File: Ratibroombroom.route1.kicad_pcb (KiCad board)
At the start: 2 copper layers, 46 x 60 mm, 112 parts, among them J1 Conn_01x02_Male, J10 Conn_01x04_Male, J11 Conn_01x04_Male, J2 Conn_01x02_Male, J3 Conn_01x10_Male, J5 Conn_01x02_Male, J6 Conn_01x02_Male, J8 Conn_01x04_Male, J9 Conn_01x04_Male, Q1 IRLML6344, Q10 S8050, Q11 IRF7416PbF, Q2 IRLML6344, Q3 IRLML6344, Q4 IRLML6344, Q5 PT12-21B/TR8, Q6 PT12-21B/TR8, Q7 PT12-21B/TR8, Q8 PT12-21B/TR8, Q9 IRLML6344, SW1 B3U, SW2 B3U, SW3 PCM12, U1 AZ1117-3.3, U2 DRV8835, U3 AS5145B-HSST, U4 MPU-9250, U5 STM32F405RGTx, U6 AS5145B-HSST, U7 DRV8835, U8 L6932D1.2TR, U9 L6932D1.2TR, Y1 8MHZ

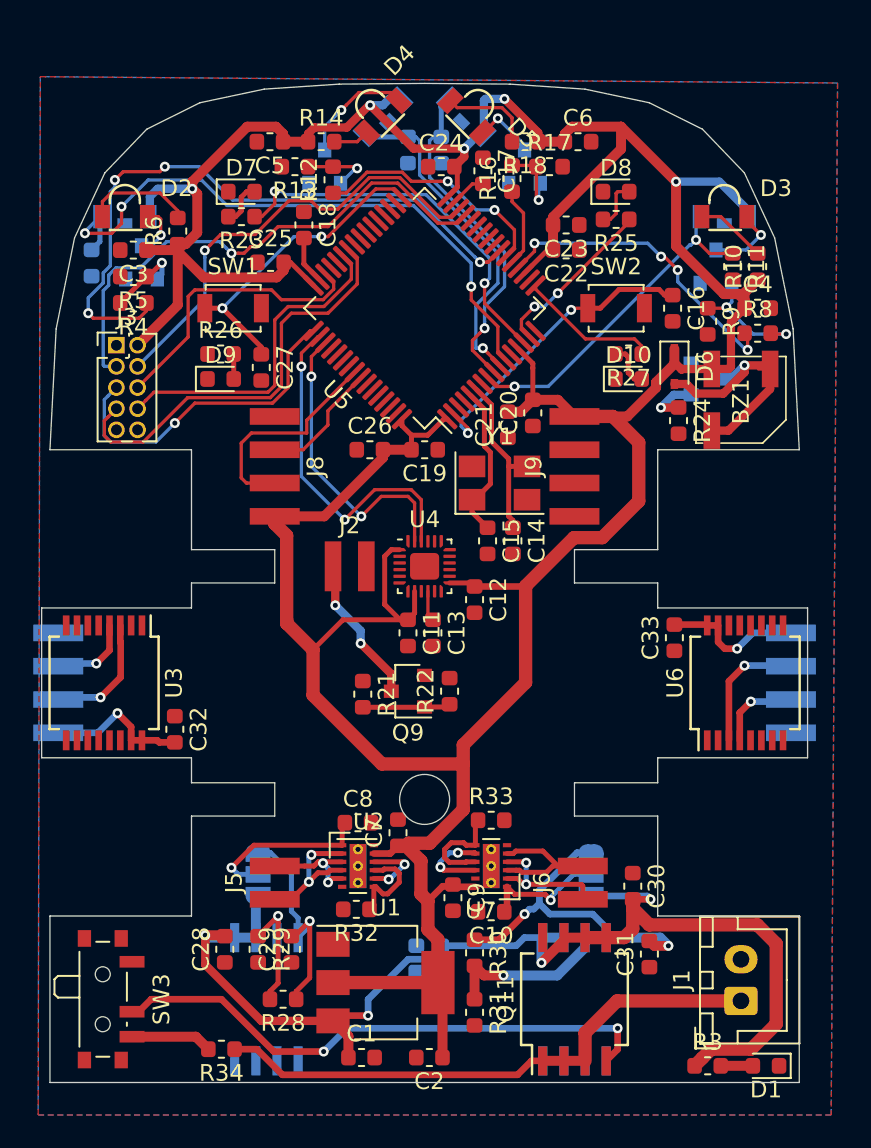
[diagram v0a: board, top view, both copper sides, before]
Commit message: Partial PCB routing
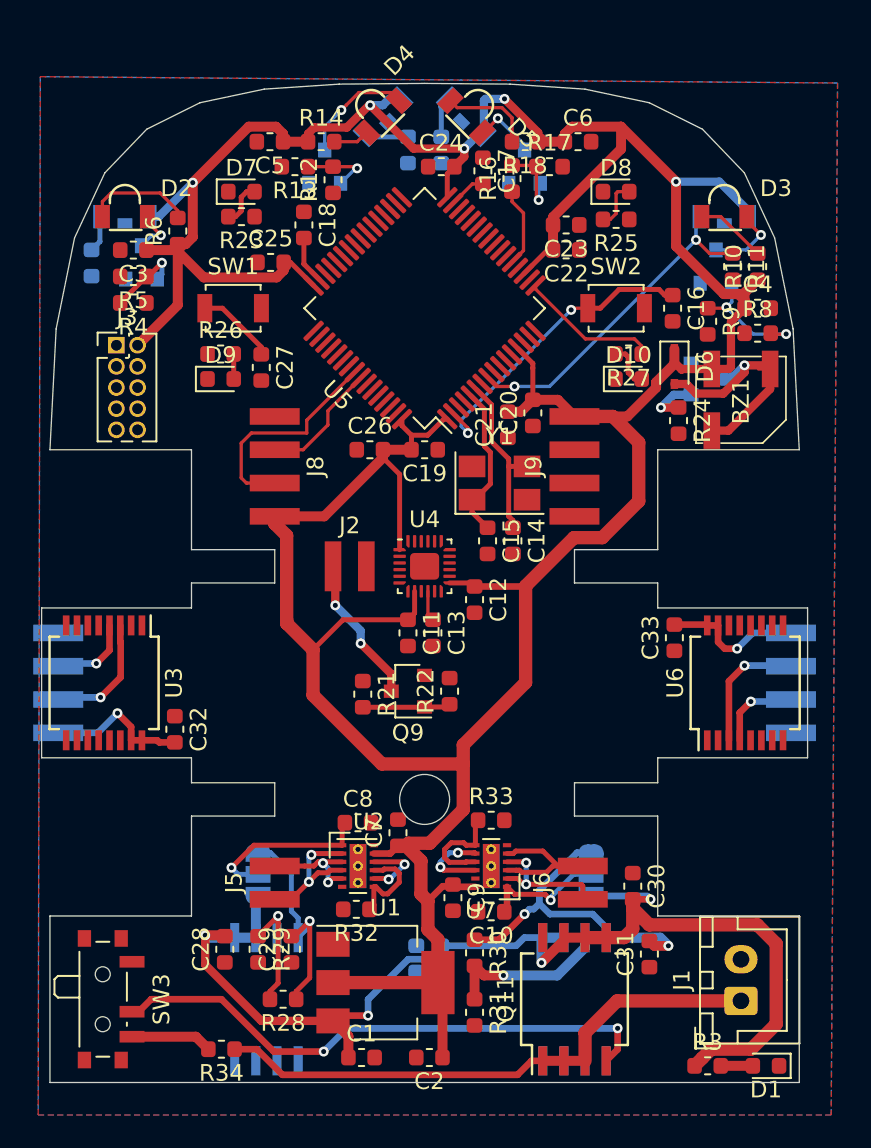
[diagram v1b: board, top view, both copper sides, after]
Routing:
- net /TX_FRONT_L: track 39.1 -> 0.00 mm, vias 4 -> 0
- net /RX_FRONT_L: track 37.5 -> 2.21 mm, vias 3 -> 0
- net /I2C_SCL: track 31.8 -> 0.00 mm, vias 1 -> 0
- net /I2C_SDA: track 27.3 -> 0.00 mm, vias 1 -> 0
- net /SERIAL_TX: track 25.7 -> 0.00 mm
- net /LED_1: track 23.0 -> 0.00 mm, vias 2 -> 0
- net /IMU_CS: track 20.7 -> 0.00 mm, vias 2 -> 0
- net /SERIAL_RX: track 20.0 -> 0.00 mm
- net /SWCLK: track 19.9 -> 0.00 mm, vias 1 -> 0
- net /TX_FRONT_R: track 18.8 -> 0.00 mm, vias 4 -> 0
- net /IMU_SCK: track 18.2 -> 0.00 mm, vias 2 -> 0
- net /RX_SIDE_R: track 20.4 -> 2.46 mm, vias 1 -> 0
- net /RX_SIDE_L: track 20.3 -> 2.62 mm, vias 1 -> 0
- net /SWDIO: track 17.3 -> 0.00 mm
- net /TX_SIDE_L: track 14.6 -> 0.00 mm, vias 2 -> 0
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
